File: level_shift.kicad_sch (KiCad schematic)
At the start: 2 parts, among them U2 CD40109B

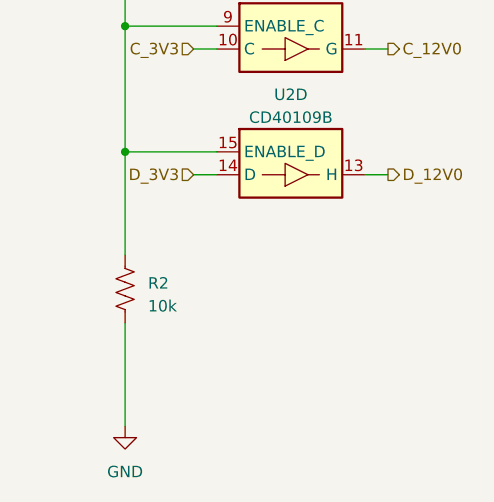
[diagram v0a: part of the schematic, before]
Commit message: built out power supplies, added datasheets
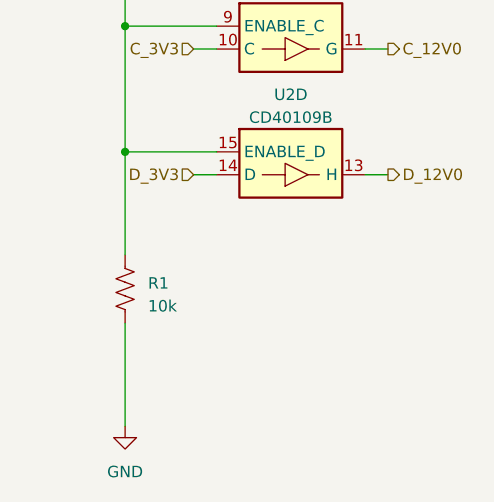
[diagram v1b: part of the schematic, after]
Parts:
- renumbered R2 to R1
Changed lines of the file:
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@@
   (symbol (lib_id "Device:R_US") (at 121.92 137.16 0) (unit 1)
     (in_bom yes) (on_board yes) (dnp no) (fields_autoplaced)
-    (property "Reference" "R2" (at 124.46 136.525 0)
+    (property "Reference" "R1" (at 124.46 136.525 0)
       (effects (font (size 1.27 1.27)) (justify left))
     )
@@
     (instances
       (project "nixie_clock_rev2"
-        (path "/0fc2f476-9e20-4198-a623-ece581a79a9a/793331c8-0196-4fce-8ed4-8422aae7d169"
-          (reference "R2") (unit 1)
-        )
         (path "/0fc2f476-9e20-4198-a623-ece581a79a9a/1bbc3371-b7a7-47c3-b6ef-e4da4bb5ac32"
           (reference "R1") (unit 1)
@@
     (instances
       (project "nixie_clock_rev2"
-        (path "/0fc2f476-9e20-4198-a623-ece581a79a9a/793331c8-0196-4fce-8ed4-8422aae7d169"
-          (reference "U2") (unit 1)
-        )
         (path "/0fc2f476-9e20-4198-a623-ece581a79a9a/1bbc3371-b7a7-47c3-b6ef-e4da4bb5ac32"
           (reference "U2") (unit 1)
@@
     (instances
       (project "nixie_clock_rev2"
-        (path "/0fc2f476-9e20-4198-a623-ece581a79a9a/793331c8-0196-4fce-8ed4-8422aae7d169"
+        (path "/0fc2f476-9e20-4198-a623-ece581a79a9a/1bbc3371-b7a7-47c3-b6ef-e4da4bb5ac32"
           (reference "U2") (unit 5)
         )
-        (path "/0fc2f476-9e20-4198-a623-ece581a79a9a/1bbc3371-b7a7-47c3-b6ef-e4da4bb5ac32"
-          (reference "U2") (unit 5)
-        )
       )
     )
@@
     (instances
       (project "nixie_clock_rev2"
-        (path "/0fc2f476-9e20-4198-a623-ece581a79a9a/793331c8-0196-4fce-8ed4-8422aae7d169"
+        (path "/0fc2f476-9e20-4198-a623-ece581a79a9a/1bbc3371-b7a7-47c3-b6ef-e4da4bb5ac32"
           (reference "#PWR04") (unit 1)
         )
-        (path "/0fc2f476-9e20-4198-a623-ece581a79a9a/1bbc3371-b7a7-47c3-b6ef-e4da4bb5ac32"
-          (reference "#PWR04") (unit 1)
-        )
       )
     )
@@
   (symbol (lib_id "power:GND") (at 139.7 60.96 0) (unit 1)
     (in_bom yes) (on_board yes) (dnp no) (fields_autoplaced)
-    (property "Reference" "#PWR02" (at 139.7 67.31 0)
+    (property "Reference" "#PWR03" (at 139.7 67.31 0)
       (effects (font (size 1.27 1.27)) hide)
     )
@@
     (instances
       (project "nixie_clock_rev2"
-        (path "/0fc2f476-9e20-4198-a623-ece581a79a9a/793331c8-0196-4fce-8ed4-8422aae7d169"
+        (path "/0fc2f476-9e20-4198-a623-ece581a79a9a/1bbc3371-b7a7-47c3-b6ef-e4da4bb5ac32"
+          (reference "#PWR03") (unit 1)
+        )
+      )
+    )
+  )
+  (symbol (lib_id "power:+3.3V") (at 135.89 40.64 0) (unit 1)
+    (in_bom yes) (on_board yes) (dnp no) (fields_autoplaced)
+    (property "Reference" "#PWR02" (at 135.89 44.45 0)
+      (effects (font (size 1.27 1.27)) hide)
+    )
+    (property "Value" "+3.3V" (at 135.89 36.83 0)
+      (effects (font (size 1.27 1.27)))
+    )
+    (property "Footprint" "" (at 135.89 40.64 0)
+      (effects (font (size 1.27 1.27)) hide)
+    )
+    (property "Datasheet" "" (at 135.89 40.64 0)
+      (effects (font (size 1.27 1.27)) hide)
+    )
+    (pin "1")
+    (instances
+      (project "nixie_clock_rev2"
+        (path "/0fc2f476-9e20-4198-a623-ece581a79a9a/1bbc3371-b7a7-47c3-b6ef-e4da4bb5ac32"
           (reference "#PWR02") (unit 1)
         )
-        (path "/0fc2f476-9e20-4198-a623-ece581a79a9a/1bbc3371-b7a7-47c3-b6ef-e4da4bb5ac32"
-          (reference "#PWR03") (unit 1)
-        )
-      )
-    )
-  )
-  (symbol (lib_id "power:+3.3V") (at 135.89 40.64 0) (unit 1)
-    (in_bom yes) (on_board yes) (dnp no) (fields_autoplaced)
-    (property "Reference" "#PWR03" (at 135.89 44.45 0)
-      (effects (font (size 1.27 1.27)) hide)
-    )
-    (property "Value" "+3.3V" (at 135.89 36.83 0)
-      (effects (font (size 1.27 1.27)))
-    )
-    (property "Footprint" "" (at 135.89 40.64 0)
-      (effects (font (size 1.27 1.27)) hide)
-    )
-    (property "Datasheet" "" (at 135.89 40.64 0)
-      (effects (font (size 1.27 1.27)) hide)
-    )
-    (pin "1")
-    (instances
-      (project "nixie_clock_rev2"
-        (path "/0fc2f476-9e20-4198-a623-ece581a79a9a/793331c8-0196-4fce-8ed4-8422aae7d169"
-          (reference "#PWR03") (unit 1)
-        )
-        (path "/0fc2f476-9e20-4198-a623-ece581a79a9a/1bbc3371-b7a7-47c3-b6ef-e4da4bb5ac32"
-          (reference "#PWR02") (unit 1)
-        )
       )
     )
@@
     (instances
       (project "nixie_clock_rev2"
-        (path "/0fc2f476-9e20-4198-a623-ece581a79a9a/793331c8-0196-4fce-8ed4-8422aae7d169"
+        (path "/0fc2f476-9e20-4198-a623-ece581a79a9a/1bbc3371-b7a7-47c3-b6ef-e4da4bb5ac32"
           (reference "U2") (unit 2)
         )
-        (path "/0fc2f476-9e20-4198-a623-ece581a79a9a/1bbc3371-b7a7-47c3-b6ef-e4da4bb5ac32"
-          (reference "U2") (unit 2)
-        )
       )
     )
@@
     (instances
       (project "nixie_clock_rev2"
-        (path "/0fc2f476-9e20-4198-a623-ece581a79a9a/793331c8-0196-4fce-8ed4-8422aae7d169"
+        (path "/0fc2f476-9e20-4198-a623-ece581a79a9a/1bbc3371-b7a7-47c3-b6ef-e4da4bb5ac32"
           (reference "#PWR01") (unit 1)
         )
-        (path "/0fc2f476-9e20-4198-a623-ece581a79a9a/1bbc3371-b7a7-47c3-b6ef-e4da4bb5ac32"
-          (reference "#PWR01") (unit 1)
-        )
       )
     )
@@
     (instances
       (project "nixie_clock_rev2"
-        (path "/0fc2f476-9e20-4198-a623-ece581a79a9a/793331c8-0196-4fce-8ed4-8422aae7d169"
+        (path "/0fc2f476-9e20-4198-a623-ece581a79a9a/1bbc3371-b7a7-47c3-b6ef-e4da4bb5ac32"
           (reference "U2") (unit 3)
         )
-        (path "/0fc2f476-9e20-4198-a623-ece581a79a9a/1bbc3371-b7a7-47c3-b6ef-e4da4bb5ac32"
-          (reference "U2") (unit 3)
-        )
       )
     )
@@
     (instances
       (project "nixie_clock_rev2"
-        (path "/0fc2f476-9e20-4198-a623-ece581a79a9a/793331c8-0196-4fce-8ed4-8422aae7d169"
+        (path "/0fc2f476-9e20-4198-a623-ece581a79a9a/1bbc3371-b7a7-47c3-b6ef-e4da4bb5ac32"
           (reference "U2") (unit 4)
-        )
-        (path "/0fc2f476-9e20-4198-a623-ece581a79a9a/1bbc3371-b7a7-47c3-b6ef-e4da4bb5ac32"
-          (reference "U2") (unit 4)

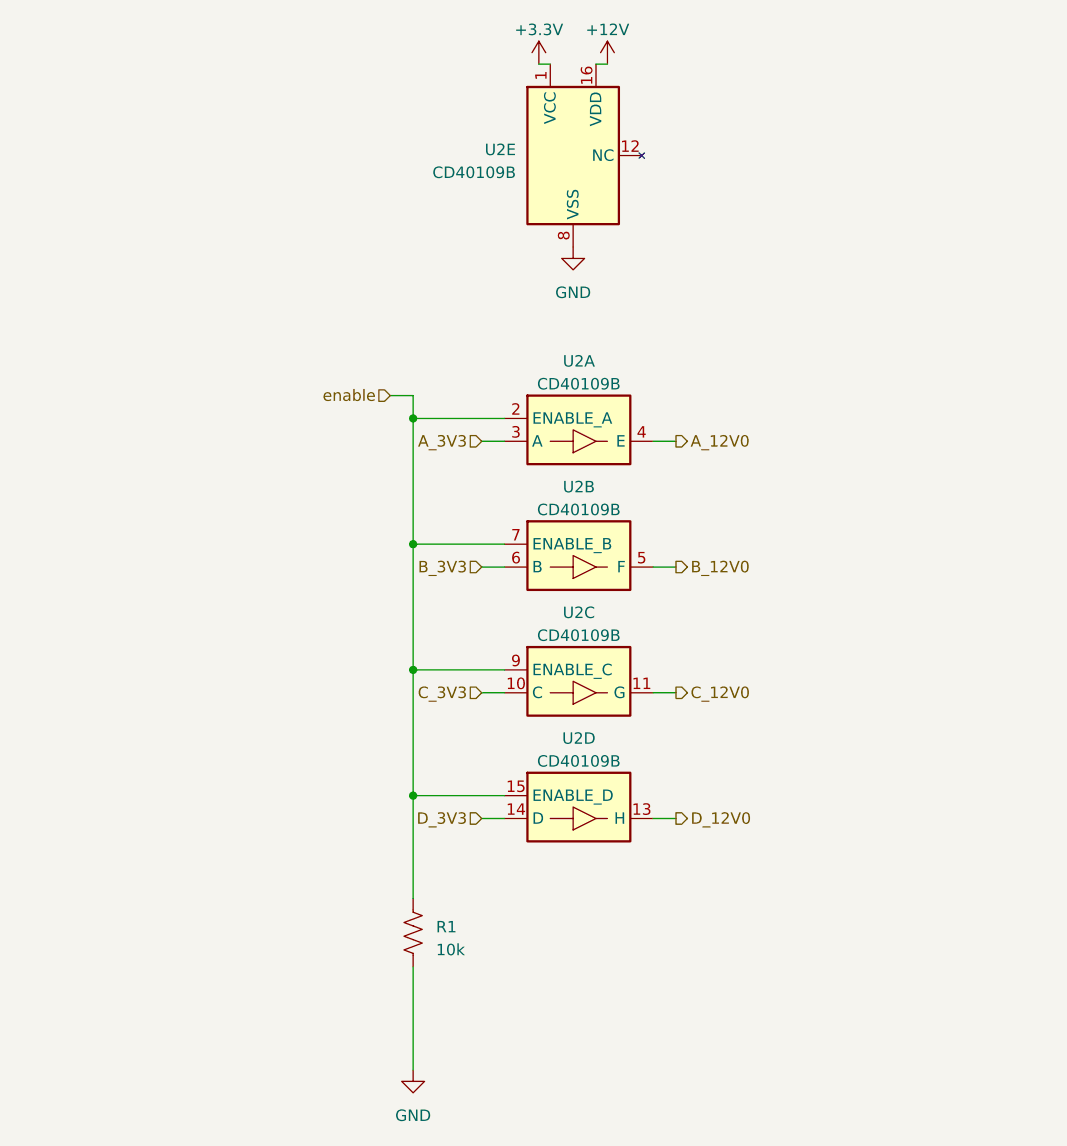
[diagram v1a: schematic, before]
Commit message: added fet-based level shifter
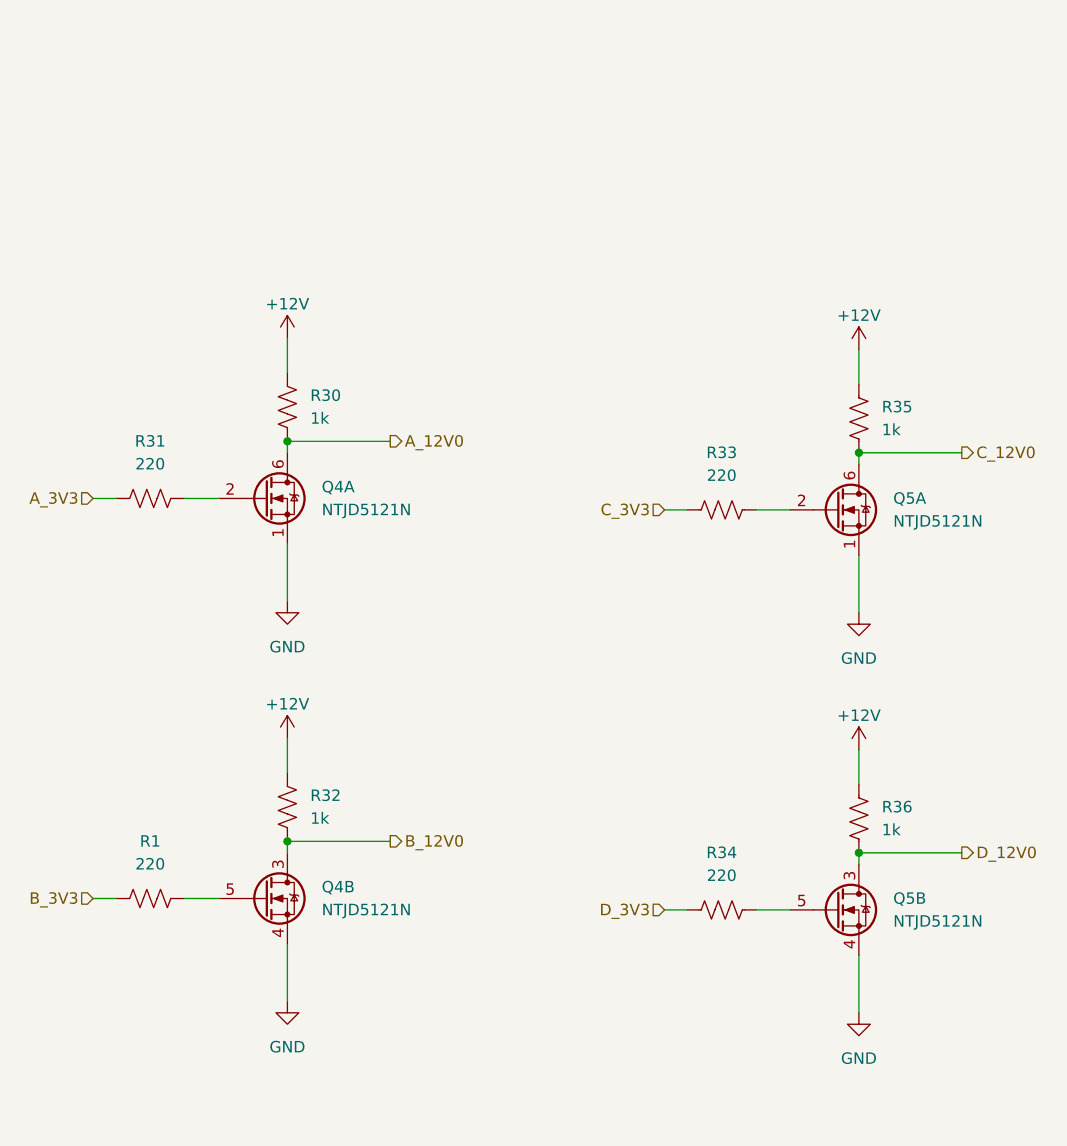
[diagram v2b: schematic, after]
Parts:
- removed U2: CD40109B, symbol nixie_lib:CD40109B
- added Q4, Q5: NTJD5121N, symbol Device:NTJD5121N
- added R30, R32, R35, R36: 1k, Resistor_SMD:R_0402_1005Metric, symbol Device:R_US
- added R31, R33, R34: 220, Resistor_SMD:R_0402_1005Metric, symbol Device:R_US
- R1: value 10k -> 220
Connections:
- net +12V: now also R30.2, R32.2, R35.2, R36.2
- net A_12V0: now also Q4.6 (D), R30.1
- net A_3V3: now also R31.2
- net B_12V0: now also Q4.3 (D), R32.1
- net B_3V3: now also R1.2
- net C_12V0: now also Q5.6 (D), R35.1
- net C_3V3: now also R33.2
- net D_12V0: now also Q5.3 (D), R36.1
- net D_3V3: now also R34.2
- net GND: now also Q4.1 (S), Q4.4 (S), Q5.1 (S), Q5.4 (S); no longer R1.2
- net enable: no longer names the net of R1.1
- net enable: now also Q4.5 (G)
- new net: Q5.2 (G), R33.1
- new net: Q5.5 (G), R34.1
- new net: Q4.2 (G), R31.1
